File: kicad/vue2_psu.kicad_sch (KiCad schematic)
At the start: 63 parts, among them U1 BGFCN8

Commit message: Convert to hierarchical schematic
Add ADC, MCU, Regulator sub-schematics and a nice PDF.

Signed-off-by: Olliver Schinagl <oliver@schinagl.nl>
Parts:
- removed C80, C81: C, symbol Device:C_Small
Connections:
- net ? is gone; now on net CY2: C61.2, C62.2, C66.1, C71.2, C75.1, D10.2 (A), L3.2, R125.1, R13.1, R7.1, R8.1, U1.4 (VDD)
- net CY2: now reaches CY2.2
- net SensL1 renamed SenseL1
- net SensL2 renamed SenseL2
- net SensL3 renamed SenseL3
- net SensN renamed SenseLN
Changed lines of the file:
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@@
-    (stroke (width 0) (type default) (color 0 0 0 0))
-  )
-  (wire (pts (xy 238.76 97.79) (xy 238.76 99.06))
     (stroke (width 0) (type default) (color 0 0 0 0))
   )
@@
     (stroke (width 0) (type default) (color 0 0 0 0))
   )
-  (wire (pts (xy 238.76 104.14) (xy 238.76 105.41))
-    (stroke (width 0) (type default) (color 0 0 0 0))
-  )
   (wire (pts (xy 252.73 137.16) (xy 252.73 134.62))
     (stroke (width 0) (type default) (color 0 0 0 0))
@@
     (stroke (width 0) (type default) (color 0 0 0 0))
   )
+  (wire (pts (xy 236.22 105.41) (xy 265.43 105.41))
+    (stroke (width 0) (type default) (color 0 0 0 0))
+  )
   (wire (pts (xy 160.02 93.98) (xy 181.61 93.98))
     (stroke (width 0) (type default) (color 0 0 0 0))
@@
     (stroke (width 0) (type default) (color 0 0 0 0))
   )
-  (wire (pts (xy 236.22 105.41) (xy 238.76 105.41))
-    (stroke (width 0) (type default) (color 0 0 0 0))
-  )
   (wire (pts (xy 209.55 123.19) (xy 210.82 123.19))
     (stroke (width 0) (type default) (color 0 0 0 0))
@@
   )
   (wire (pts (xy 220.98 95.25) (xy 220.98 100.33))
-    (stroke (width 0) (type default) (color 0 0 0 0))
-  )
-  (wire (pts (xy 238.76 92.71) (xy 240.03 92.71))
     (stroke (width 0) (type default) (color 0 0 0 0))
   )
@@
     (effects (font (size 1.27 1.27)) (justify right bottom))
   )
-  (label "?" (at 240.03 92.71 0)
+  (label "?" (at 264.795 105.41 0)
     (effects (font (size 1.27 1.27)) (justify left bottom))
   )
@@
     (effects (font (size 1.27 1.27)) (justify right bottom))
   )
-  (hierarchical_label "SensL2" (shape input) (at 144.78 67.31 0)
+  (hierarchical_label "SenseL2" (shape output) (at 144.78 67.31 0)
     (effects (font (size 1.27 1.27)) (justify left))
   )
-  (hierarchical_label "SensL1" (shape input) (at 144.78 82.55 0)
+  (hierarchical_label "CY2" (shape output) (at 265.43 105.41 0)
     (effects (font (size 1.27 1.27)) (justify left))
   )
-  (hierarchical_label "SensL3" (shape input) (at 144.78 52.07 0)
+  (hierarchical_label "SenseL1" (shape output) (at 144.78 82.55 0)
     (effects (font (size 1.27 1.27)) (justify left))
   )
-  (hierarchical_label "SensN" (shape input) (at 144.78 109.22 0)
+  (hierarchical_label "SenseL3" (shape output) (at 144.78 52.07 0)
+    (effects (font (size 1.27 1.27)) (justify left))
+  )
+  (hierarchical_label "SenseLN" (shape output) (at 144.78 109.22 0)
     (effects (font (size 1.27 1.27)) (justify left))
   )
@@
     )
     (property "Datasheet" "~" (id 3) (at 252.73 111.76 0)
-      (effects (font (size 1.27 1.27)) hide)
-    )
-    (pin "1")
-    (pin "2")
-  )
-  (symbol (lib_id "Device:C_Small") (at 238.76 95.25 0) (unit 1)
-    (in_bom yes) (on_board yes) (fields_autoplaced)
-    (property "Reference" "C81" (id 0) (at 241.3 93.9862 0)
-      (effects (font (size 1.27 1.27)) (justify left))
-    )
-    (property "Value" "C" (id 1) (at 241.3 96.5262 0)
-      (effects (font (size 1.27 1.27)) (justify left))
-    )
-    (property "Footprint" "" (id 2) (at 238.76 95.25 0)
-      (effects (font (size 1.27 1.27)) hide)
-    )
-    (property "Datasheet" "~" (id 3) (at 238.76 95.25 0)
       (effects (font (size 1.27 1.27)) hide)
     )
@@
     (pin "7")
   )
-  (symbol (lib_id "Device:C_Small") (at 238.76 101.6 0) (unit 1)
-    (in_bom yes) (on_board yes) (fields_autoplaced)
-    (property "Reference" "C80" (id 0) (at 241.3 100.3362 0)
-      (effects (font (size 1.27 1.27)) (justify left))
-    )
-    (property "Value" "C" (id 1) (at 241.3 102.8762 0)
-      (effects (font (size 1.27 1.27)) (justify left))
-    )
-    (property "Footprint" "" (id 2) (at 238.76 101.6 0)
-      (effects (font (size 1.27 1.27)) hide)
-    )
-    (property "Datasheet" "~" (id 3) (at 238.76 101.6 0)
-      (effects (font (size 1.27 1.27)) hide)
-    )
-    (pin "1")
-    (pin "2")
-  )
   (symbol (lib_id "Device:R") (at 139.7 67.31 90) (unit 1)

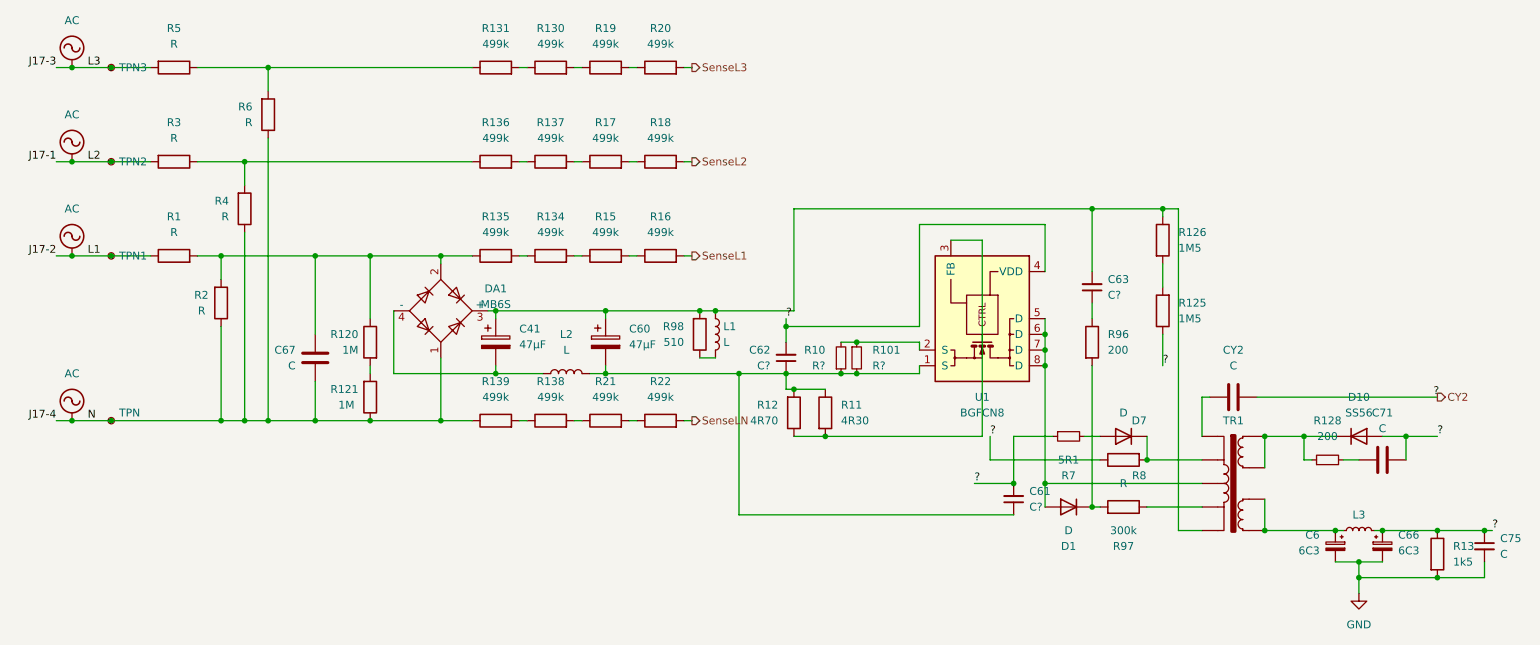
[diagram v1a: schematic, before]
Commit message: Update schematic
As described in https://github.com/emporia-vue-local/esphome/discussions/173#discussioncomment-6137086

Thank you @g3gg0!

Also this ends up upgrading the project to Kicad 7
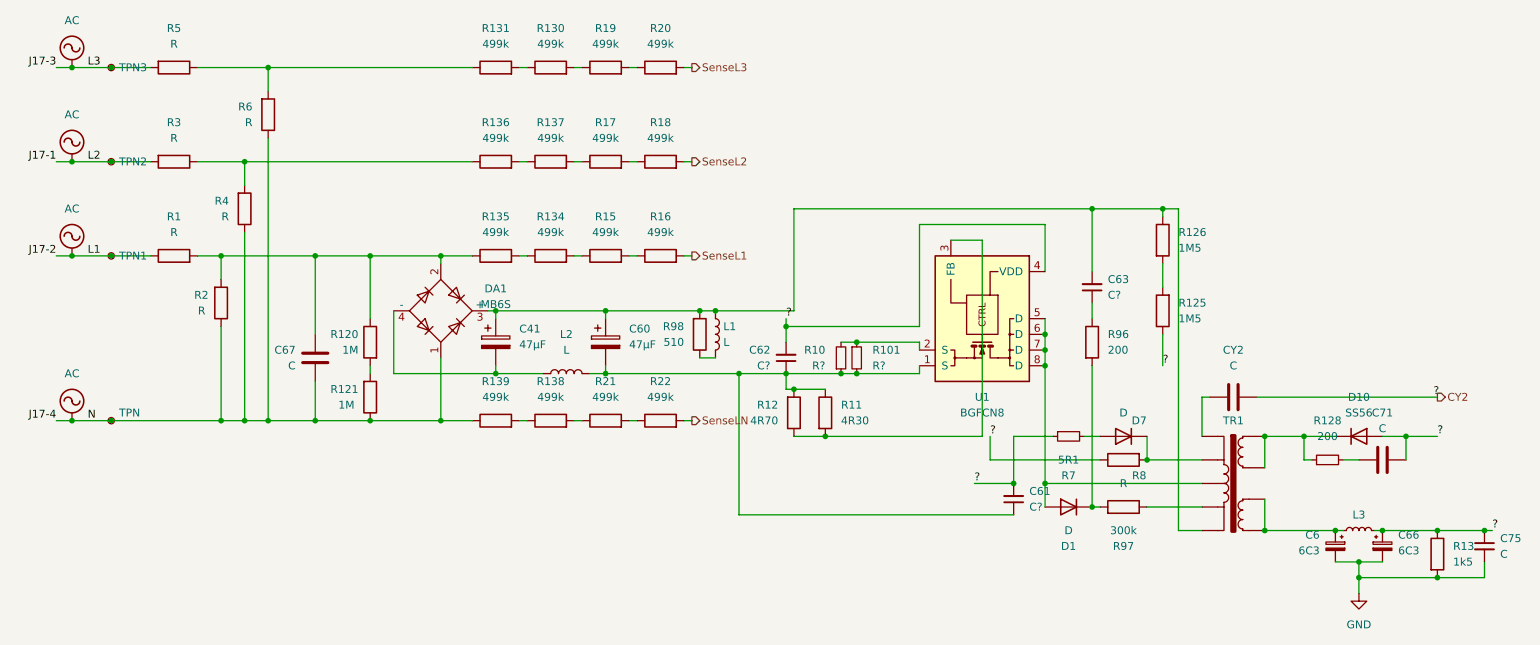
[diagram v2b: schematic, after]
